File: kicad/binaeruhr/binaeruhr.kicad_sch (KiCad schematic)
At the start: 33 parts, among them U1 ATmega48PA-A, Y1 Crystal

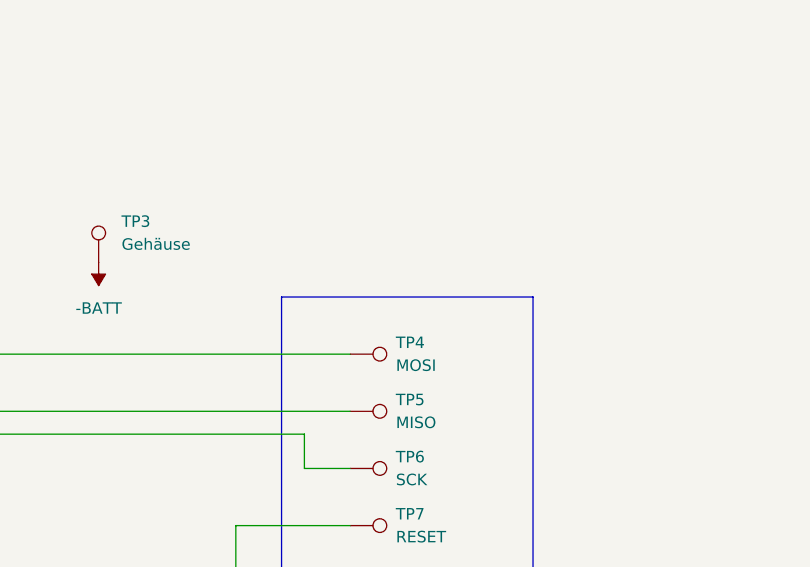
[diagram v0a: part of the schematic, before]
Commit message: add missing text above box
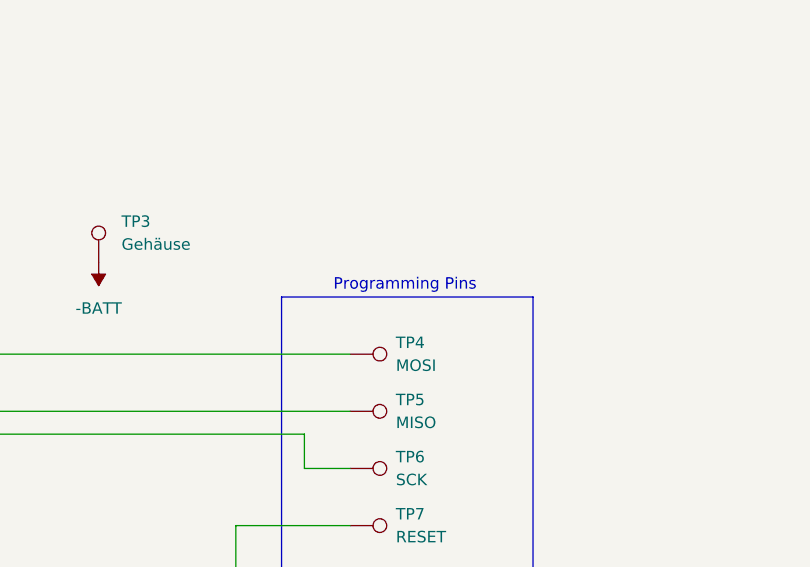
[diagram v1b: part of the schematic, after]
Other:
- note added: "Programming Pins"
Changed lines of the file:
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@@
+		)
+	)
+	(text "Programming Pins"
+		(exclude_from_sim no)
+		(at 216.916 55.88 0)
+		(effects
+			(font
+				(size 1.27 1.27)
+			)
 		)
 	)
